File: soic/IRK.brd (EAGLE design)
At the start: 142.9 x 39.7 mm, 44 parts, among them CON1 FE16-1, IC1 PIC18F25K50, Q1 MMBT2222A, Q2 2N7002, Q3 2N7002, Q4 TSOP4838, Q5 MMBT3906

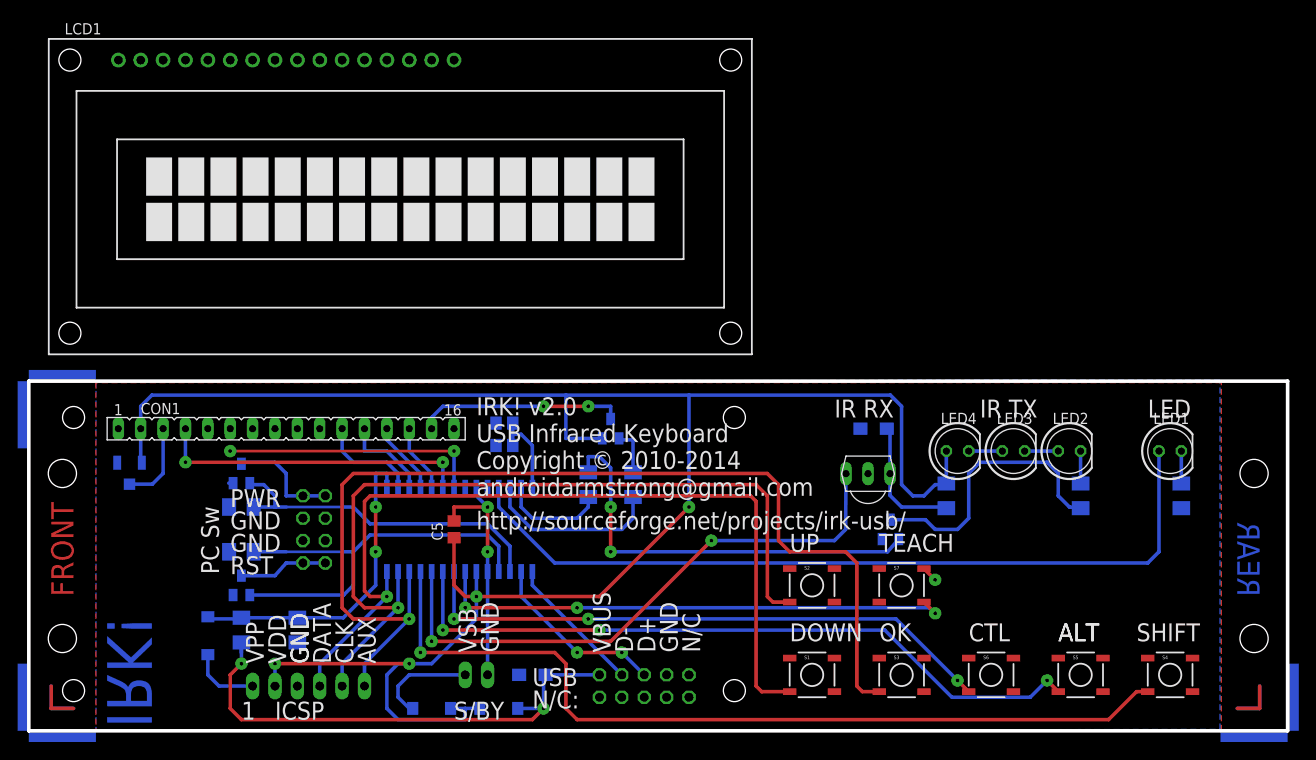
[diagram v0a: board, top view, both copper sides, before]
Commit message: Reworked SMD board layout
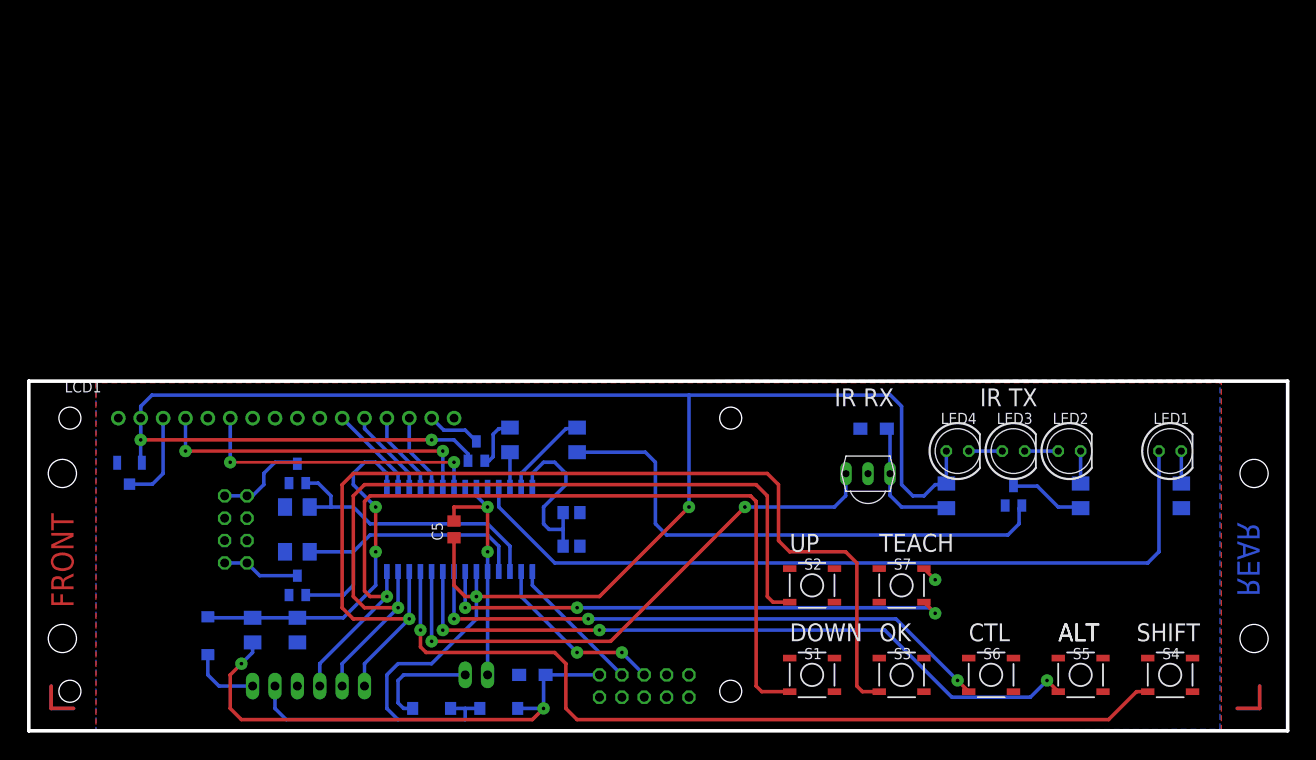
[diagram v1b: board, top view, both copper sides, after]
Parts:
- removed CON1: FE16-1, con-lsta-with16:FE16
- removed U$1, U$2, U$3: (no value), marks:ANGLE-ARROW-NW1
- LCD1: value HD44780 -> TUXGR_16X2_R2; device display-lcd:TUXGR_16X2_R2 -> offboard:TUXGR_16X2_R2
- moved LCD1 40.6 mm to (42.2, 20.0)
- moved Q5 15.5 mm to (50.8, 31.8)
- moved R8 14.9 mm to (54.6, 33.0)
- moved Q1 14.5 mm to (111.8, 26.7)
- moved C4 13.7 mm to (61.6, 21.0), turned to 180 degrees
- moved C3 12.7 mm to (61.6, 24.8), turned to 180 degrees
- moved JP1 8.89 mm to (23.5, 22.9)
- moved Q2 6.35 mm to (30.5, 29.2)
- moved Q3 6.35 mm to (30.5, 16.5)
- moved R6 6.35 mm to (30.5, 25.4)
- moved R7 6.35 mm to (30.5, 20.3)
- moved R5 5.24 mm to (62.2, 33.0), turned to 90 degrees
- moved R9 1.27 mm to (25.4, 11.4)
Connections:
- net +5V: no longer CON1.2
- net GND: no longer CON1.1, CON1.10, CON1.16, CON1.5, CON1.7, CON1.8, CON1.9
- net N$1: no longer CON1.11
- net N$2: no longer CON1.12
- net N$3: no longer CON1.13
- net N$31: no longer CON1.15
- net N$4: no longer CON1.14
- net N$5: no longer CON1.4
- net N$6: no longer CON1.6
- net N$7: no longer CON1.3
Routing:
- net +5V: track 225.5 -> 254.4 mm
- net N$30: track 31.6 -> 8.66 mm
- net N$31: track 23.6 -> 6.17 mm, vias 2 -> 0
- net N$34: track 20.2 -> 3.98 mm
- net N$29: track 47.7 -> 60.9 mm, vias 2 -> 0
- net N$9: track 48.2 -> 35.3 mm
- net N$19: track 10.4 -> 19.5 mm
- net N$37: track 38.5 -> 32.2 mm
- net N$8: track 36.6 -> 41.1 mm
- net N$6: track 29.5 -> 33.3 mm
- net N$10: track 66.5 -> 64.3 mm
- net N$22: track 12.7 -> 10.6 mm
- net N$28: track 12.1 -> 10.1 mm
- net GND: track 30.4 -> 29.0 mm
- net N$11: track 10.2 -> 8.85 mm
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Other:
- board text added: "IRK! v2.0 USB Infrared Keyboard (C) 2010-2014 androidarmstrong@gmail.com"
- board text removed: "IRK!"
- board text removed: "IRK! v2.0 USB Infrared Keyboard Copyright © 2010-2014 androidarmstrong@gmail.com"
- board text removed: "LED"
- board text removed: "N/C:"
- board text removed: "PC Sw"
- board text removed: "S/BY"
- board text removed: "USB"
